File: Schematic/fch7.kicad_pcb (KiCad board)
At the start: 2 copper layers, 42 x 42 mm, 151 parts, among them IC1 MP9943AGQ-Z, IC2 MP9943AGQ-Z, IC3 STM32H743VIT6, IC4 ICM-42688-P, IC5 MPU-6500, J10 PIN2216, J11 PIN2216, J12 PIN2216, J2 PIN2216, J3 PIN2216, J4 PIN2216, J5 PIN2216, J6 PIN2216, J7 PIN2216, J8 PIN2216, J9 PIN2216, SW1 TS24CA, SW2 TS24CA, U1 ME6217C33M5G, U10 HDGC1002WR-S-4P, U11 HDGC1002WR-S-4P, U12 E28-2G4M27SX, U13 ESP-01F-2M, U14 HDGC1002WR-S-4P, U15 HDGC1002WR-S-6P, U16 HDGC1002WR-S-8P, U17 HDGC1002WR-S-8P, U2 ME6217C33M5G, U3 LDO-1.8v, U4 QMC5883L, U5 SPL06-001, U6 CSNP1GCR01-BOW, U7 HDGC1002WR-S-4P, U8 HDGC1002WR-S-4P, U9 HDGC1002WR-S-4P, Y1 8MHz

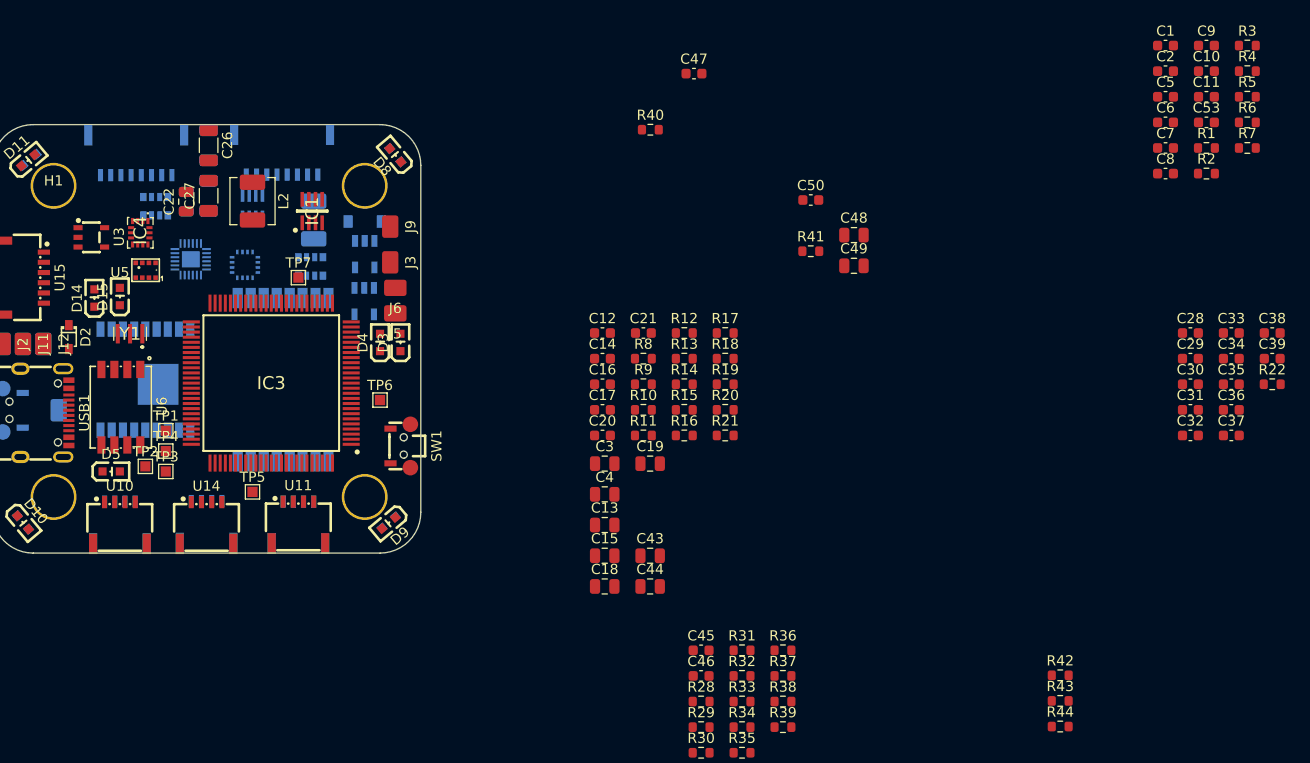
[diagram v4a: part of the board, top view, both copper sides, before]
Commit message: Update clearance and width parameters in fch7.kicad_pro
- Increased min_clearance from 0.0 to 0.2 for improved design rules.
- Set min_track_width from 0.0 to 0.2 to enhance track integrity.
- Adjusted min_via_diameter from 0.5 to 0.8 for better via performance.
- Updated via_drill size from 0.3 to 0.4 for improved manufacturability.
- Added new differential pair settings for GND and POWER with specific parameters for clearance, track width, and via dimensions.
- Changed net_format_name to "KiCad" for better compatibility.
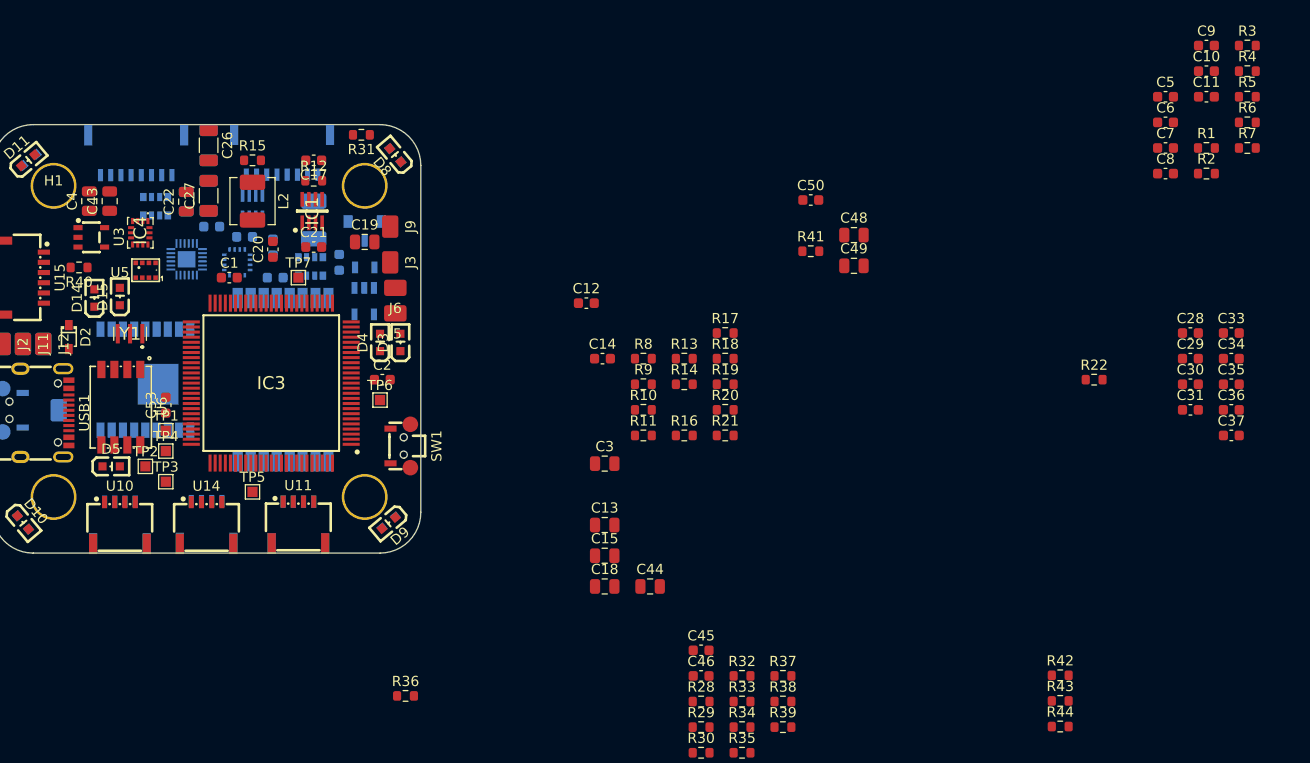
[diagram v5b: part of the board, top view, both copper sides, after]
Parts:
- C16, C32, C38, C39, C47: moved to B.Cu
- moved C53 105.7 mm to (80.0, 87.5), turned to 90 degrees
- moved C38 101.2 mm to (87.7, 71.0)
- moved C32 98.1 mm to (84.5, 70.0)
- moved C39 98.1 mm to (90.7, 75.0)
- moved C1 94.5 mm to (86.2, 75.0)
- moved C2 82.5 mm to (101.2, 85.0)
- moved C43 63.4 mm to (74.5, 67.5), turned to 90 degrees
- moved R31 62.8 mm to (99.2, 61.0), turned to 180 degrees
- moved C4 58.1 mm to (72.5, 67.5), turned to 90 degrees
- moved R40 57.6 mm to (71.5, 74.0), turned to 180 degrees
- moved R15 48.9 mm to (88.5, 63.5)
- moved C47 39.4 mm to (97.0, 73.5), turned to 90 degrees
- moved R12 39.3 mm to (94.5, 65.5)
- moved C17 37.4 mm to (94.5, 63.5), turned to 180 degrees
- moved R36 37.3 mm to (103.5, 116.0)
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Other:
- copper layers 2 -> 4

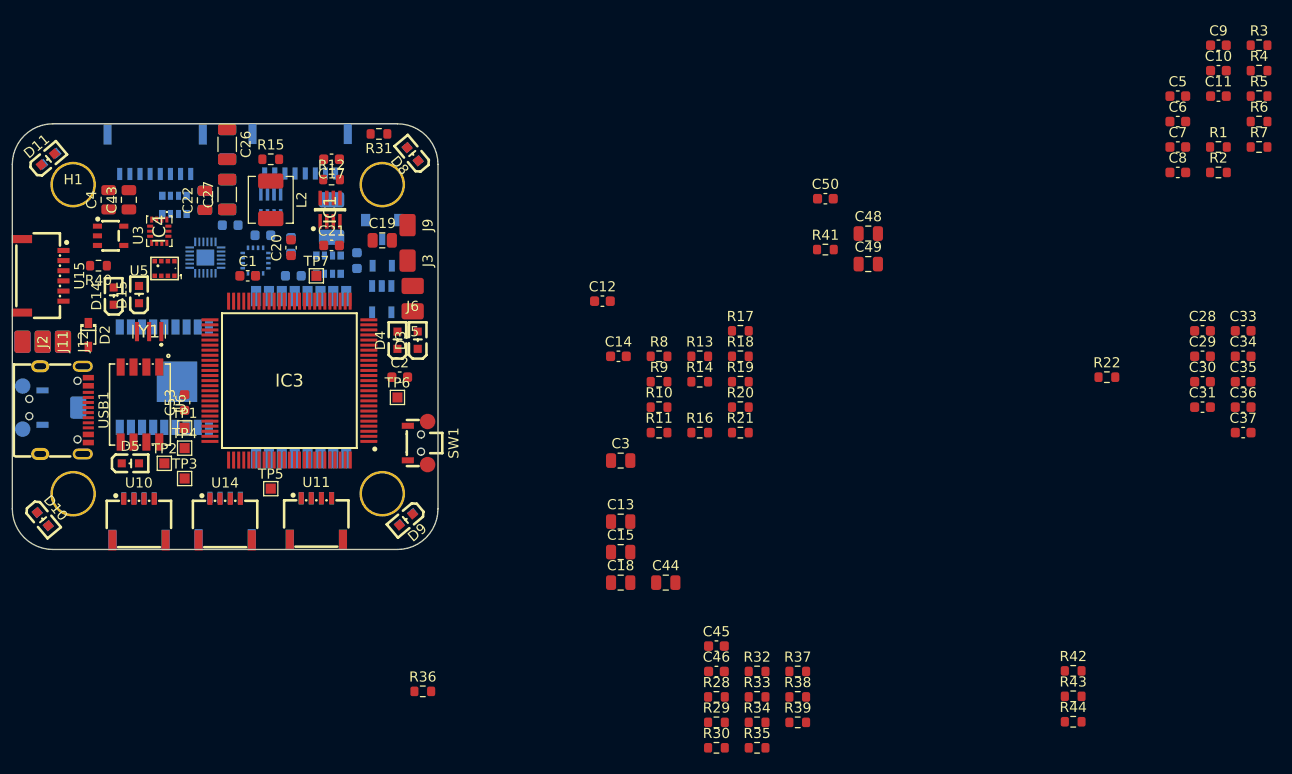
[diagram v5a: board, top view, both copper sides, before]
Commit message: still progressing on placing capacitance
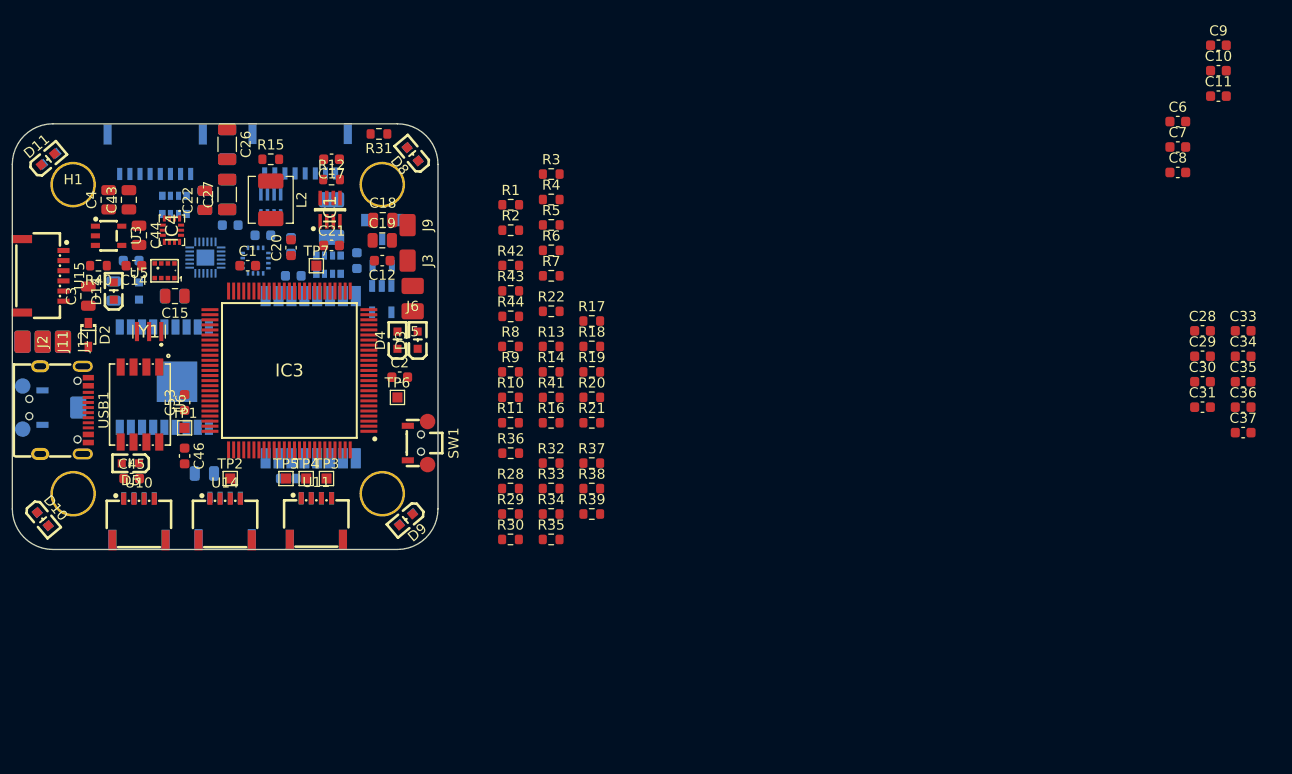
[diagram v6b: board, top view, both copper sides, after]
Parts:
- C13, C48, C49, C5, C50, D15: moved to B.Cu
- moved C5 104.5 mm to (74.7, 73.5), turned to 180 degrees
- moved C48 74.7 mm to (73.0, 76.5), turned to 90 degrees
- moved R3 71.0 mm to (116.2, 65.0)
- moved R4 71.0 mm to (116.2, 67.5)
- moved R5 71.0 mm to (116.2, 70.0)
- moved R6 71.0 mm to (116.2, 72.5)
- moved R7 71.0 mm to (116.2, 75.0)
- moved R1 70.1 mm to (112.2, 68.0)
- moved R2 70.1 mm to (112.2, 70.5)
- moved C49 68.5 mm to (79.0, 77.0), turned to 180 degrees
- moved R42 68.4 mm to (112.2, 74.0)
- moved R43 68.4 mm to (112.2, 76.5)
- moved R44 68.4 mm to (112.2, 79.0)
- moved C44 62.3 mm to (75.5, 71.0), turned to -90 degrees
- moved C45 60.0 mm to (74.8, 95.0)
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
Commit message: finised capacitor placement
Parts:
- C10, C11, C28, C29, C31, C36, C37, C6, C7, C8, C9: moved to B.Cu
- moved C31 113.2 mm to (68.7, 69.5)
- moved C37 112.5 mm to (72.0, 94.3), turned to 90 degrees
- moved C36 110.6 mm to (74.0, 94.2), turned to 90 degrees
- moved C9 109.0 mm to (74.8, 72.0)
- moved C10 108.4 mm to (74.8, 70.5)
- moved C11 107.9 mm to (74.8, 69.0)
- moved C33 107.3 mm to (78.0, 94.2), turned to -90 degrees
- moved C6 106.8 mm to (71.7, 70.5), turned to 180 degrees
- moved C7 106.7 mm to (71.7, 72.0), turned to 180 degrees
- moved C8 106.6 mm to (71.7, 73.5), turned to 180 degrees
- moved C28 105.8 mm to (75.5, 94.2), turned to -90 degrees
- moved C34 105.2 mm to (80.0, 95.8), turned to 90 degrees
- moved C30 104.8 mm to (77.2, 67.0)
- moved C29 104.0 mm to (77.0, 94.2), turned to -90 degrees
- moved C35 102.3 mm to (82.5, 94.5), turned to 180 degrees
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
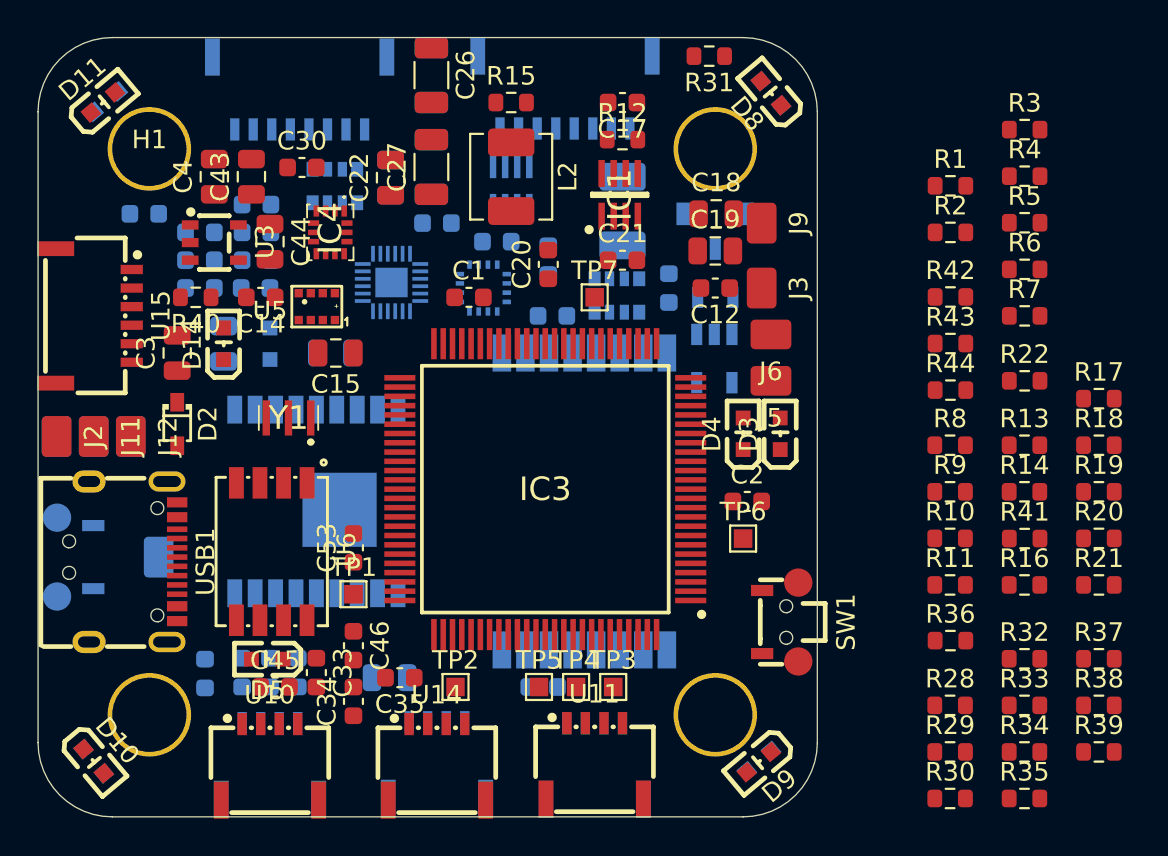
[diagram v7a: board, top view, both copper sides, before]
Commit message: progress on placing components
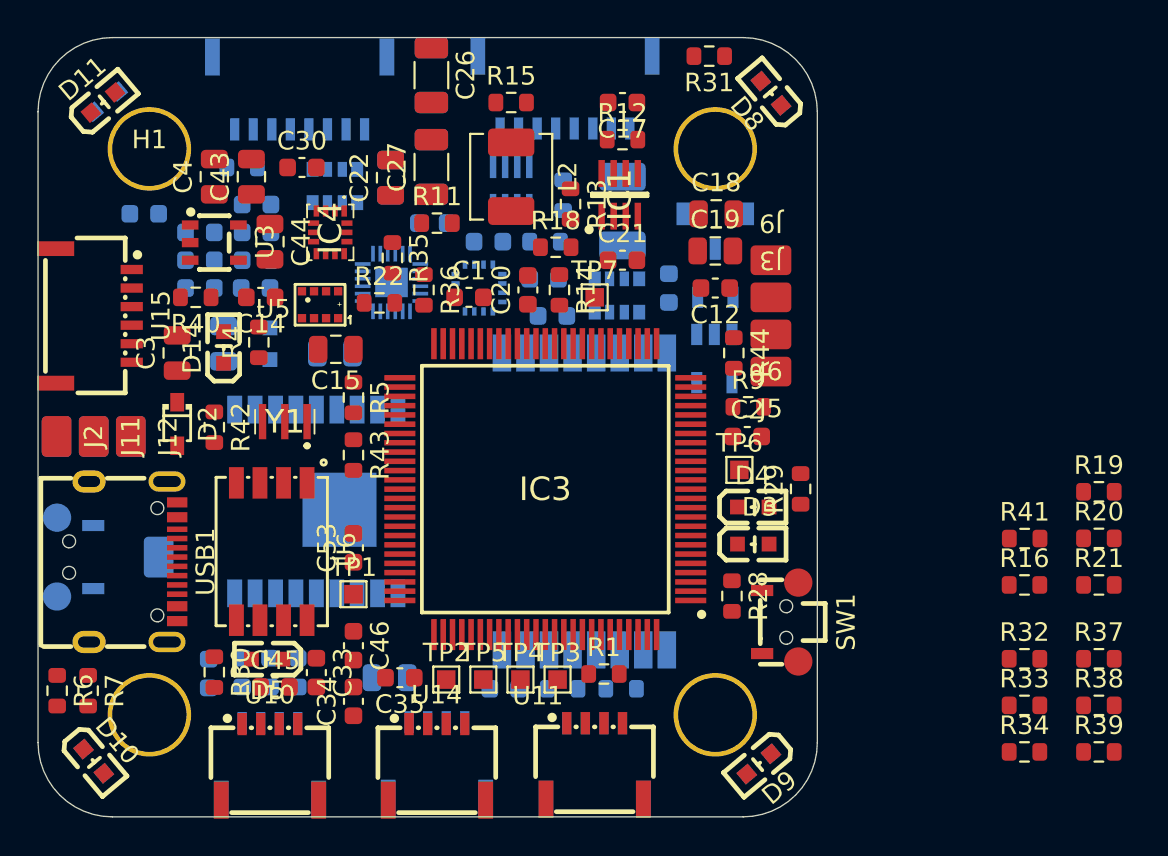
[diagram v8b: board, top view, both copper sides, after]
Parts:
- R10, R17, R2, R3, R8: moved to B.Cu
- moved R6 56.9 mm to (64.0, 95.2), turned to -90 degrees
- moved R7 54.4 mm to (65.7, 95.2), turned to -90 degrees
- moved R35 44.8 mm to (82.1, 71.9), turned to -90 degrees
- moved R4 42.2 mm to (74.9, 76.4), turned to 90 degrees
- moved R8 41.0 mm to (74.0, 67.0), turned to 180 degrees
- moved R42 40.3 mm to (72.5, 81.0), turned to -90 degrees
- moved R30 40.2 mm to (72.5, 94.2), turned to -90 degrees
- moved R5 37.4 mm to (80.0, 79.4), turned to -90 degrees
- moved R3 37.2 mm to (94.4, 95.1), turned to 180 degrees
- moved R22 35.0 mm to (81.4, 74.3)
- moved R36 34.1 mm to (83.8, 73.6), turned to -90 degrees
- moved R11 33.8 mm to (84.5, 70.0)
- moved R43 32.7 mm to (80.0, 82.5), turned to -90 degrees
- moved R2 32.3 mm to (91.3, 95.1), turned to 180 degrees
- moved R1 32.3 mm to (93.5, 94.3)
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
